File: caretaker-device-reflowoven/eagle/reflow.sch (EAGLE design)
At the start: 30 parts, among them IC1 ATmega328P-20PU, IC2 XBEE-1B1, IC3 MCP1702-3302, Q1 16MHz, T1 TIP110

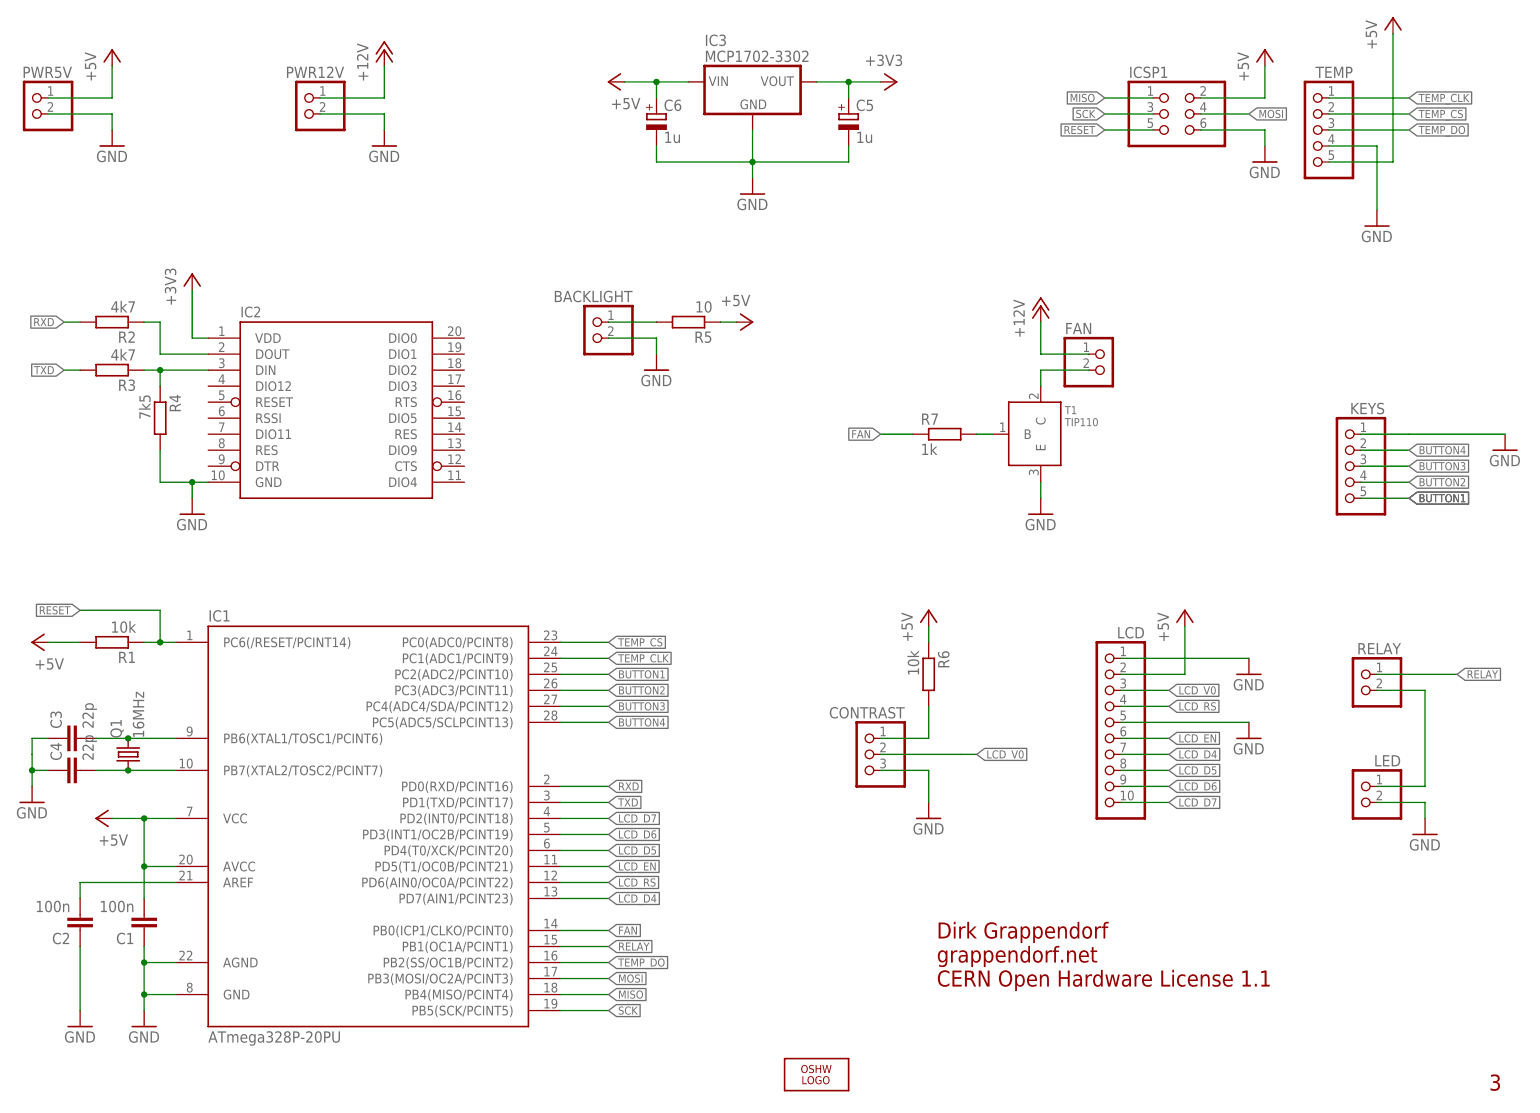
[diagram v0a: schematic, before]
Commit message: feat: Convert the XBee Reflow Oven device to a WLAN device fix: LCD flickering
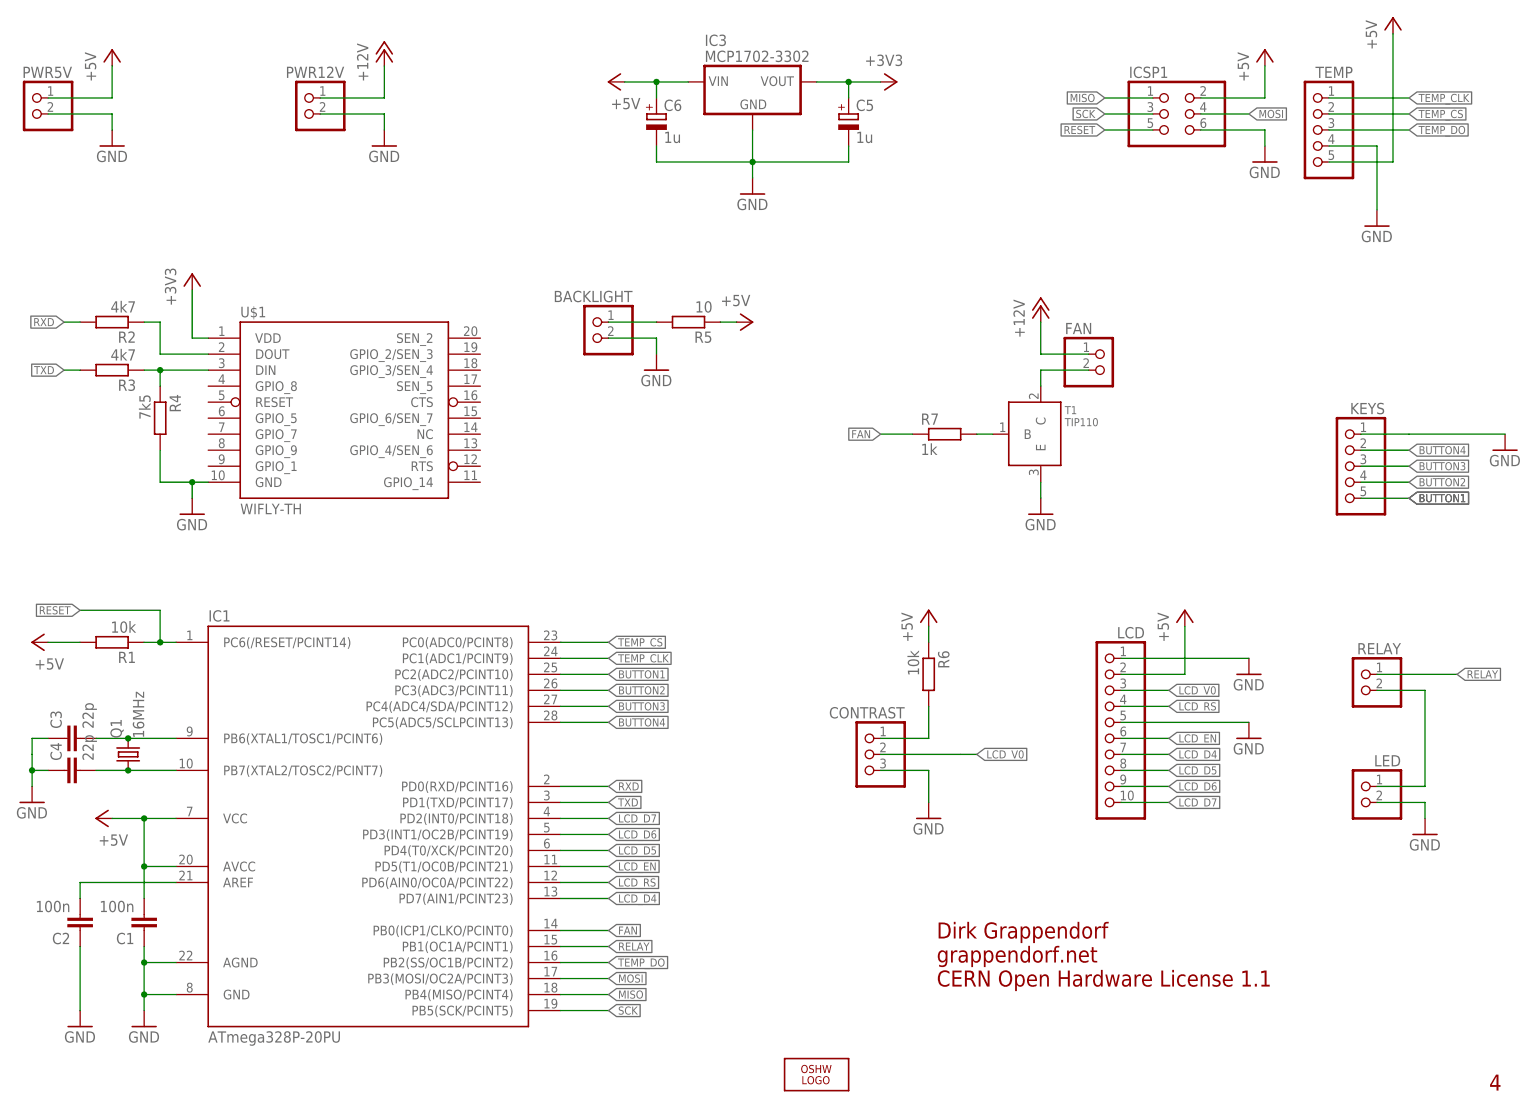
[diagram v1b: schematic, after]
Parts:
- removed IC2: XBEE-1B1, SparkFun:XBEE-1B1
- added U$1: WIFLY-TH, grapelabs:WIFLY-TH
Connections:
- net +3V3: now also U$1.VDD; no longer IC2.VDD
- net GND: now also U$1.GND; no longer IC2.GND
- net N$4: now also U$1.DIN; no longer IC2.DIN
- net N$5: now also U$1.DOUT; no longer IC2.DOUT
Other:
- note added: "4"
- note removed: "3"
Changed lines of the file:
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@@
 <?xml version="1.0" encoding="utf-8"?>
 <!DOCTYPE eagle SYSTEM "eagle.dtd">
-<eagle version="6.4">
+<eagle version="6.5.0">
 <drawing>
 <settings>
@@
 <part name="KEYS" library="pinhead" deviceset="PINHD-1X5" device=""/>
 <part name="FRAME1" library="frames" deviceset="DINA4_L" device=""/>
-<part name="IC2" library="SparkFun" deviceset="XBEE-1" device="B1" value=""/>
 <part name="IC1" library="atmega8" deviceset="ATMEGA48/88/168-PU" device="" value="ATmega328P-20PU"/>
 <part name="Q1" library="crystal" deviceset="CRYSTAL" device="HC49U-V" value="16MHz"/>
@@
 <part name="P+9" library="supply1" deviceset="+12V" device=""/>
 <part name="LOGO1" library="OSHW" deviceset="OSHW_LOGO_10MIL" device="X0350-NT-BOTTOM"/>
+<part name="U$1" library="grapelabs" deviceset="WIFLY" device="-TH"/>
 </parts>
 <sheets>
@@
 <plain>
 <text x="163.83" y="31.75" size="2.54" layer="94">Dirk Grappendorf</text>
-<text x="251.46" y="7.62" size="2.54" layer="94">3</text>
+<text x="251.46" y="7.62" size="2.54" layer="94">4</text>
 <text x="163.83" y="27.94" size="2.54" layer="94">grappendorf.net</text>
 <text x="163.83" y="24.13" size="2.54" layer="94">CERN Open Hardware License 1.1</text>
@@
 <instance part="FRAME1" gate="G$1" x="0" y="0"/>
 <instance part="FRAME1" gate="G$2" x="162.56" y="0"/>
-<instance part="IC2" gate="G$1" x="68.58" y="116.84"/>
 <instance part="IC1" gate="1" x="73.66" y="50.8"/>
 <instance part="Q1" gate="G$1" x="35.56" y="60.96" rot="R90"/>
@@
 <instance part="P+9" gate="1" x="180.34" y="132.08"/>
 <instance part="LOGO1" gate="G$1" x="144.78" y="10.16"/>
+<instance part="U$1" gate="G$1" x="68.58" y="116.84"/>
 </instances>
 <busses>
@@
 <wire x1="45.72" y1="101.6" x2="45.72" y2="104.14" width="0.1524" layer="91"/>
 <junction x="45.72" y="104.14"/>
-<pinref part="IC2" gate="G$1" pin="GND"/>
 <pinref part="R4" gate="G$1" pin="2"/>
 <pinref part="SUPPLY5" gate="1" pin="GND"/>
+<pinref part="U$1" gate="G$1" pin="GND"/>
 </segment>
 <segment>
@@
 <wire x1="40.64" y1="119.38" x2="40.64" y2="121.92" width="0.1524" layer="91"/>
 <junction x="40.64" y="121.92"/>
-<pinref part="IC2" gate="G$1" pin="DIN"/>
 <pinref part="R3" gate="G$1" pin="1"/>
 <pinref part="R4" gate="G$1" pin="1"/>
+<pinref part="U$1" gate="G$1" pin="DIN"/>
 </segment>
 </net>
@@
 <wire x1="40.64" y1="124.46" x2="48.26" y2="124.46" width="0.1524" layer="91"/>
 <pinref part="R2" gate="G$1" pin="1"/>
-<pinref part="IC2" gate="G$1" pin="DOUT"/>
+<pinref part="U$1" gate="G$1" pin="DOUT"/>
 </segment>
 </net>
@@
 <wire x1="45.72" y1="127" x2="48.26" y2="127" width="0.1524" layer="91"/>
 <pinref part="+3V1" gate="G$1" pin="+3V3"/>
-<pinref part="IC2" gate="G$1" pin="VDD"/>
-</segment>
-<segment>
+<pinref part="U$1" gate="G$1" pin="VDD"/>
+</segment>
+<segment>
